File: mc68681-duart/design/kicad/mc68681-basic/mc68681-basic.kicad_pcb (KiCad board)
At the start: 4 copper layers, 80 x 110 mm, 34 parts, among them IC1 68681, IC2 74HCT245, IC3 74HCT245, IC4 74HCT245, IC5 74126, IC6 IC6_DECO.PLD, IC7 IC7_UART_.PLD, J1 Conn_02x32_Odd_Even, J2 EXTBUS, J3 UART_A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

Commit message: Fix a couple of issues...
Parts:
- added R2: 10K, Resistor_THT:R_Axial_DIN0207_L6.3mm_D2.5mm_P10.16mm_Horizontal, F.Cu at (92.8, 127.0)
- IC5: value 74126 -> 74125
- moved R1 5.85 mm to (78.0, 147.2)
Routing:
- net IRQ: track 109.9 -> 116.1 mm
- net IOSEL: track 35.7 -> 38.0 mm, vias 2 -> 1
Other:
- board text added: "74HCT125"
- board text added: "74HCT245"
- board text added: "DTACK Enable"
- board text added: "EXT Enable"
- board text added: "GAL - DECODER"
- board text added: "GAL - GLUE"
- board text added: "Revision 1 - July 2020"
- board text added: "VCC - A"
- board text added: "VCC - B"
- board text removed: "Revision 0 - Prototype"

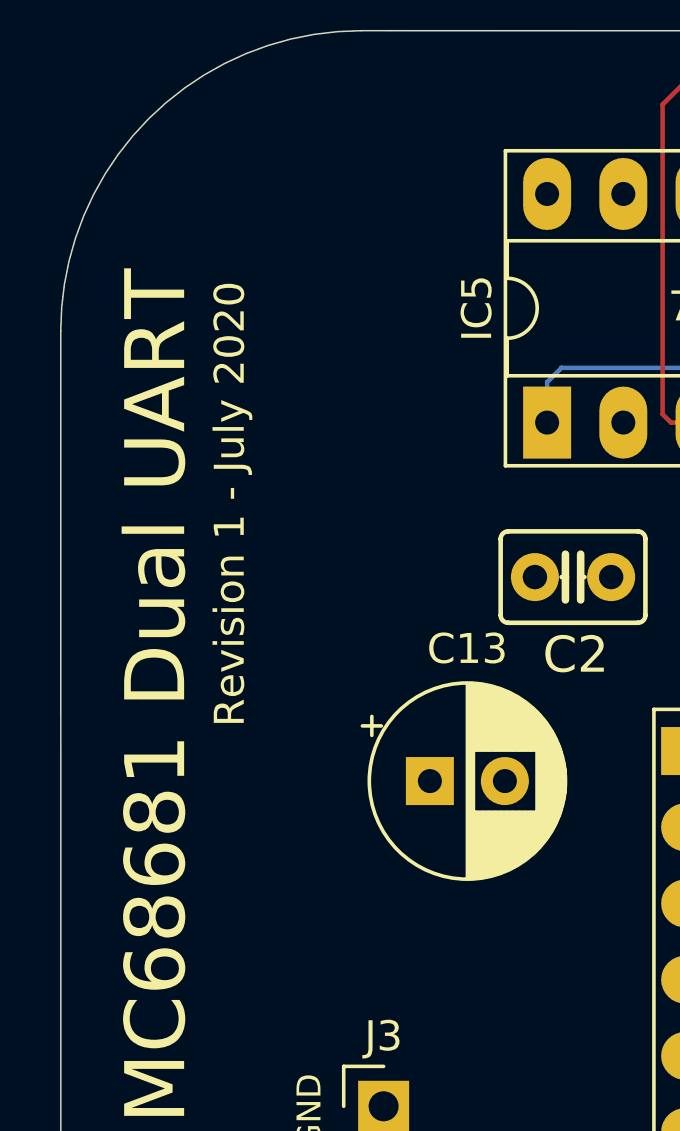
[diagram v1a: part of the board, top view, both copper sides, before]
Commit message: Fix incorrect direction for EXT drivers
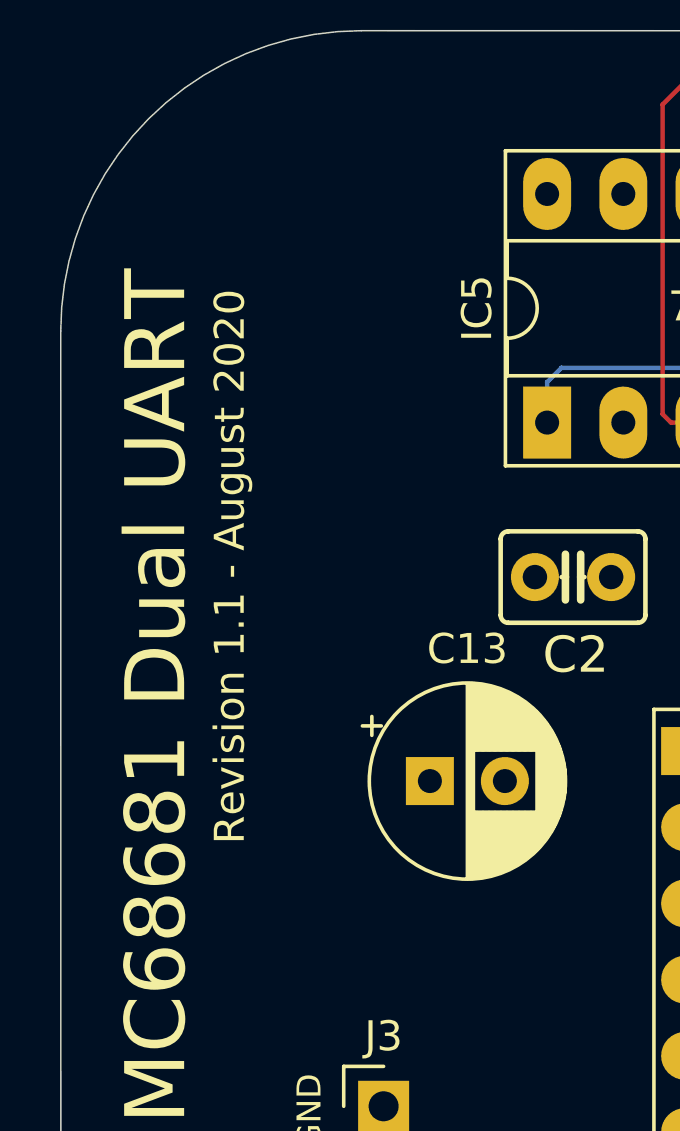
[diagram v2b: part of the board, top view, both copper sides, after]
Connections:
- IC3 pad 1: GND -> VCC
- IC4 pad 1: GND -> VCC
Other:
- board text added: "Revision 1.1 - August 2020"
- board text removed: "Revision 1 - July 2020"
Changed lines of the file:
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@@
   )
   (setup
-    (last_trace_width 0.15)
+    (last_trace_width 0.25)
     (user_trace_width 0.15)
     (user_trace_width 0.4)
@@
       (net 22 RXDB))
     (pad 1 thru_hole rect (at 0 0 90) (size 2.4 1.6) (drill 0.8) (layers *.Cu *.Mask)
-      (net 1 GND))
+      (net 2 VCC))
     (model ${KISYS3DMOD}/Package_DIP.3dshapes/DIP-20_W7.62mm_Socket.wrl
       (at (xyz 0 0 0))
@@
       (net 57 BOP7))
     (pad 1 thru_hole rect (at 0 0 90) (size 2.4 1.6) (drill 0.8) (layers *.Cu *.Mask)
-      (net 1 GND))
+      (net 2 VCC))
     (model ${KISYS3DMOD}/Package_DIP.3dshapes/DIP-20_W7.62mm_Socket.wrl
       (at (xyz 0 0 0))
@@
     (effects (font (size 0.8 0.8) (thickness 0.15)))
   )
-  (gr_text "Revision 1 - July 2020" (at 56.425 61.764285 90) (layer F.SilkS)
+  (gr_text "Revision 1.1 - August 2020" (at 56.425 63.85 90) (layer F.SilkS)
     (effects (font (size 1 1) (thickness 0.15)))
   )

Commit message: Fixes for 1.2 mainboard
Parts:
- C3, C5: value 33pF -> 7pF
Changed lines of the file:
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@@
       (effects (font (size 1.2065 1.2065) (thickness 0.12065)) (justify left bottom))
     )
-    (fp_text value 33pF (at -3.556 -2.032 -180) (layer F.Fab)
+    (fp_text value 7pF (at -3.556 -2.032 -180) (layer F.Fab)
       (effects (font (size 1.2065 1.2065) (thickness 0.12065)) (justify left bottom))
     )
@@
       (effects (font (size 1.2065 1.2065) (thickness 0.12065)) (justify left bottom))
     )
-    (fp_text value 33pF (at -3.556 -2.032 -180) (layer F.Fab)
+    (fp_text value 7pF (at -3.556 -2.032 -180) (layer F.Fab)
       (effects (font (size 1.2065 1.2065) (thickness 0.12065)) (justify left bottom))
     )
